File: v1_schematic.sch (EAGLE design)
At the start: 75 parts, among them IC1 PCA82C250, IC2 FT232RL, IC3 SP3223EBP, IC4 MAX481CPA, Q1 25MHz, Q2 32.768kHz, T1 ST02-3.5MM, X1 MINI-USB-32005-201

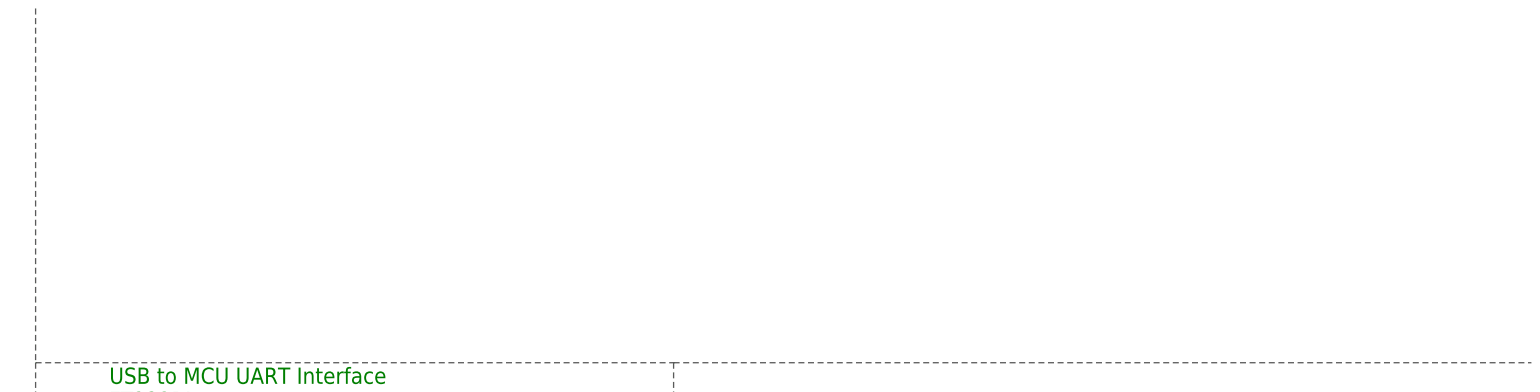
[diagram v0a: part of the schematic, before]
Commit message: Power Conversion and References
- Completed power supply conversion for 5V (VCC) and 3V3.
- Added STM32F407VETx pinout image for design reference.
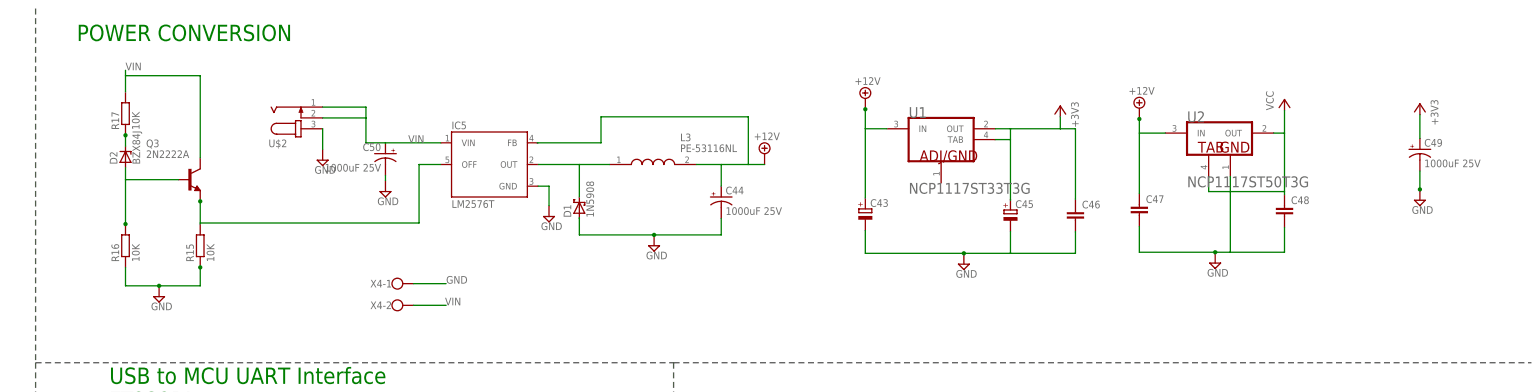
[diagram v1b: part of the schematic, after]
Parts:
- added C43, C45: (no value), rcl:CPOL-EU153CLV-1014
- added C44, C49, C50: 1000uF 25V, rcl:CPOL-USE5-6
- added C46, C47, C48: (no value), SparkFun-Capacitors:CAP0603-CAP
- added D1: 1N5908, diode:1N5908
- added D2: BZX84J, NXP_60_26022015:BZX84J
- added IC5: LM2576T, v-reg-3-new:LM2576T
- added L3: PE-53116NL, PE-53116NL:PE-53116NL
- added Q3: 2N2222A, transistor-npn:2N2222A
- added R15, R16, R17: 10K, rcl:R-EU_R0805
- added U$2: (no value), con-jack:JACK-PLUG1
- added U1: ON_SEMICONDUCTOR_NCP1117ST33T3GON_SEMICONDUCTOR_NCP1117ST33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, ON Semiconductor - NCP1117ST33T3G:ON_SEMICONDUCTOR_NCP1117ST33T3GON_SEMICONDUCTOR_NCP1117ST33T3G_0_0
- added U2: ON_SEMICONDUCTOR_NCP1117ST50T3GON_SEMICONDUCTOR_NCP1117ST50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, ON Semiconductor - NCP1117ST50T3G:ON_SEMICONDUCTOR_NCP1117ST50T3GON_SEMICONDUCTOR_NCP1117ST50T3G_0_2
- added X4: (no value), con-wago-500:W237-102
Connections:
- new net +12V: C43.+, C44.+, C47.1, L3.2, U1.IN, U2.IN
- new net N$30: D2.A, Q3.B, R16.2
- new net N$32: Q3.E, R15.2
- new net N$35: D2.C, R17.1
- new net N$36: IC5.OFF
- new net N$41: D1.C, IC5.OUT, L3.1
- new net VIN: C50.+, IC5.VIN, Q3.C, R17.2, U$2.1, U$2.2, X4-2.KL
- net +3V3: now also C46.1, C49.+, U1.OUT, U1.TAB
- net GND: now also C43.-, C44.-, C45.-, C46.2, C47.2, C48.2, C49.-, C50.-, D1.A, IC5.GND, R15.1, R16.1, U$2.3, U2.GND, X4-1.KL
- net VCC: now also C48.1, U2.OUT, U2.TAB
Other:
- note added: "POWER CONVERSION"

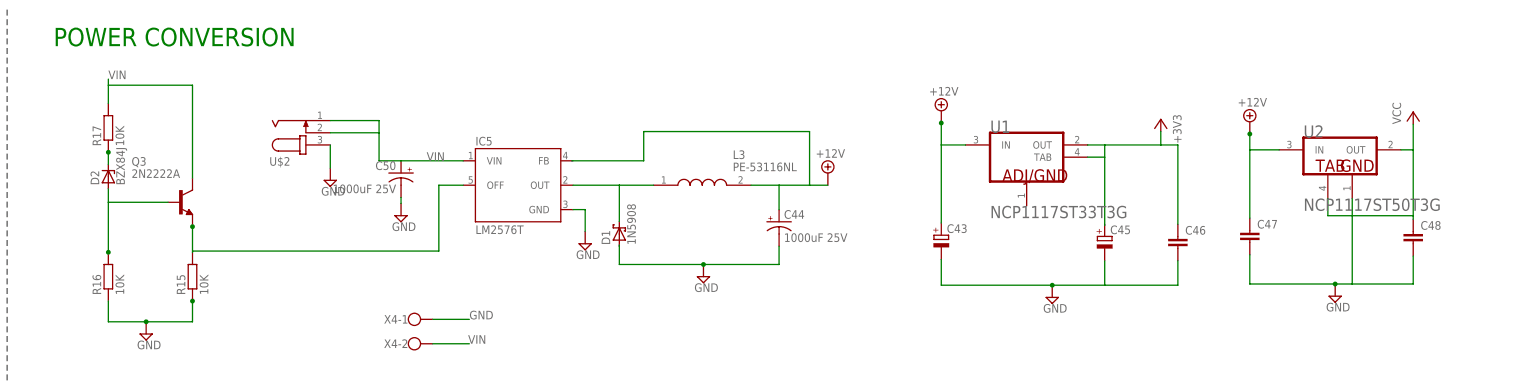
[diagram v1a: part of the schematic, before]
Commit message: Corrections
- Values for various passive parts adjusted.
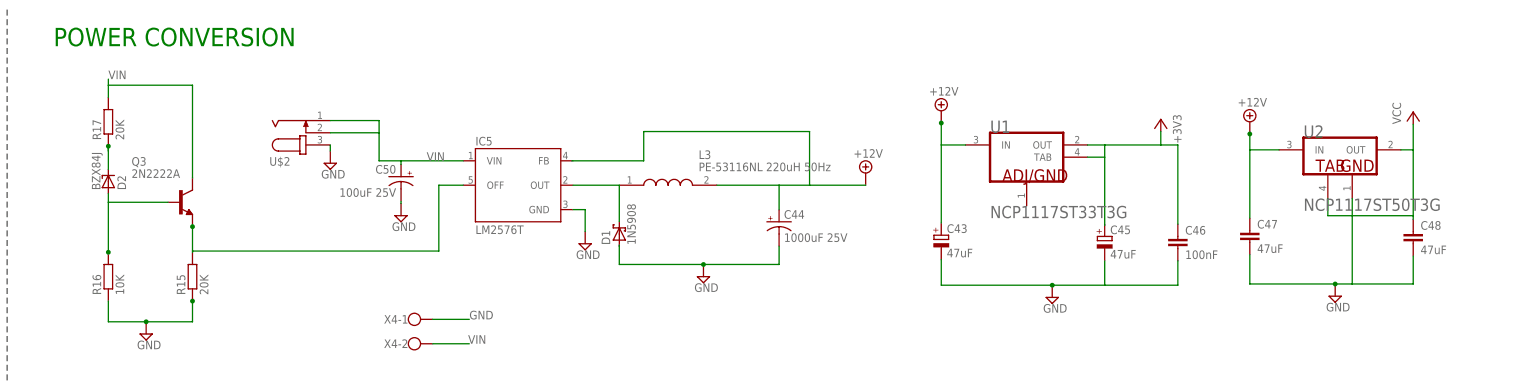
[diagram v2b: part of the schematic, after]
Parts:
- C43, C45, C47, C48: value (none) -> 47uF
- C46: value (none) -> 100nF
- C50: value 1000uF 25V -> 100uF 25V
- L3: value PE-53116NL -> PE-53116NL 220uH 50Hz
- R15, R17: value 10K -> 20K
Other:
- moved on the sheet: C50, D2, L3, R17
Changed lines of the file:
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@@
 <part name="D1" library="diode" library_urn="urn:adsk.eagle:library:210" deviceset="1N5908" device="" package3d_urn="urn:adsk.eagle:package:43355/1"/>
 <part name="Q3" library="transistor-npn" library_urn="urn:adsk.eagle:library:398" deviceset="2N2222*" device="" package3d_urn="urn:adsk.eagle:package:28973/2" technology="A"/>
-<part name="R15" library="rcl" library_urn="urn:adsk.eagle:library:334" deviceset="R-EU_" device="R0805" package3d_urn="urn:adsk.eagle:package:23553/2" value="10K"/>
+<part name="R15" library="rcl" library_urn="urn:adsk.eagle:library:334" deviceset="R-EU_" device="R0805" package3d_urn="urn:adsk.eagle:package:23553/2" value="20K"/>
 <part name="R16" library="rcl" library_urn="urn:adsk.eagle:library:334" deviceset="R-EU_" device="R0805" package3d_urn="urn:adsk.eagle:package:23553/2" value="10K"/>
-<part name="R17" library="rcl" library_urn="urn:adsk.eagle:library:334" deviceset="R-EU_" device="R0805" package3d_urn="urn:adsk.eagle:package:23553/2" value="10K"/>
+<part name="R17" library="rcl" library_urn="urn:adsk.eagle:library:334" deviceset="R-EU_" device="R0805" package3d_urn="urn:adsk.eagle:package:23553/2" value="20K"/>
 <part name="D2" library="NXP_60_26022015" deviceset="BZX84J" device=""/>
-<part name="C43" library="rcl" library_urn="urn:adsk.eagle:library:334" deviceset="CPOL-EU" device="153CLV-1014" package3d_urn="urn:adsk.eagle:package:23406/1"/>
+<part name="C43" library="rcl" library_urn="urn:adsk.eagle:library:334" deviceset="CPOL-EU" device="153CLV-1014" package3d_urn="urn:adsk.eagle:package:23406/1" value="47uF"/>
 <part name="C44" library="rcl" library_urn="urn:adsk.eagle:library:334" deviceset="CPOL-US" device="E5-6" package3d_urn="urn:adsk.eagle:package:23368/1" value="1000uF 25V"/>
-<part name="L3" library="PE-53116NL" deviceset="PE-53116NL" device=""/>
-<part name="C45" library="rcl" library_urn="urn:adsk.eagle:library:334" deviceset="CPOL-EU" device="153CLV-1014" package3d_urn="urn:adsk.eagle:package:23406/1"/>
-<part name="C46" library="SparkFun-Capacitors" deviceset="CAP" device="0603-CAP"/>
-<part name="C47" library="SparkFun-Capacitors" deviceset="CAP" device="0603-CAP"/>
-<part name="C48" library="SparkFun-Capacitors" deviceset="CAP" device="0603-CAP"/>
+<part name="L3" library="PE-53116NL" deviceset="PE-53116NL" device="" value="PE-53116NL 220uH 50Hz"/>
+<part name="C45" library="rcl" library_urn="urn:adsk.eagle:library:334" deviceset="CPOL-EU" device="153CLV-1014" package3d_urn="urn:adsk.eagle:package:23406/1" value="47uF"/>
+<part name="C46" library="SparkFun-Capacitors" deviceset="CAP" device="0603-CAP" value="100nF"/>
+<part name="C47" library="SparkFun-Capacitors" deviceset="CAP" device="0603-CAP" value="47uF"/>
+<part name="C48" library="SparkFun-Capacitors" deviceset="CAP" device="0603-CAP" value="47uF"/>
 <part name="C49" library="rcl" library_urn="urn:adsk.eagle:library:334" deviceset="CPOL-US" device="E5-6" package3d_urn="urn:adsk.eagle:package:23368/1" value="1000uF 25V"/>
 <part name="U$2" library="con-jack" library_urn="urn:adsk.eagle:library:154" deviceset="JACK-PLUG" device="1" package3d_urn="urn:adsk.eagle:package:7494/1"/>
-<part name="C50" library="rcl" library_urn="urn:adsk.eagle:library:334" deviceset="CPOL-US" device="E5-6" package3d_urn="urn:adsk.eagle:package:23368/1" value="1000uF 25V"/>
+<part name="C50" library="rcl" library_urn="urn:adsk.eagle:library:334" deviceset="CPOL-US" device="E5-6" package3d_urn="urn:adsk.eagle:package:23368/1" value="100uF 25V"/>
 <part name="X4" library="con-wago-500" library_urn="urn:adsk.eagle:library:195" deviceset="W237-102" device="" package3d_urn="urn:adsk.eagle:package:10688/1"/>
 <part name="SUPPLY23" library="supply2" library_urn="urn:adsk.eagle:library:372" deviceset="GND" device=""/>
@@
 <instance part="R15" gate="G$1" x="-51.308" y="147.32" rot="R90"/>
 <instance part="R16" gate="G$1" x="-68.834" y="147.32" rot="R90"/>
-<instance part="R17" gate="G$1" x="-68.834" y="178.308" rot="R90"/>
-<instance part="D2" gate="G$1" x="-68.834" y="168.148" rot="R90"/>
+<instance part="R17" gate="G$1" x="-68.834" y="179.578" rot="R90"/>
+<instance part="D2" gate="G$1" x="-68.834" y="167.132" rot="MR90"/>
 <instance part="C43" gate="G$1" x="104.648" y="155.956"/>
 <instance part="C44" gate="G$1" x="70.866" y="158.75"/>
-<instance part="L3" gate="G$1" x="44.704" y="166.37"/>
+<instance part="L3" gate="G$1" x="37.592" y="166.37"/>
 <instance part="C45" gate="G$1" x="138.684" y="155.702"/>
 <instance part="C46" gate="G$1" x="153.924" y="153.162"/>
@@
 <instance part="C49" gate="G$1" x="234.696" y="169.926"/>
 <instance part="U$2" gate="G$1" x="-27.686" y="177.292" rot="MR180"/>
-<instance part="C50" gate="G$1" x="-7.874" y="168.91" rot="MR0"/>
+<instance part="C50" gate="G$1" x="-7.874" y="168.148" rot="MR0"/>
 <instance part="X4" gate="-1" x="-6.35" y="138.43"/>
 <instance part="X4" gate="-2" x="-6.35" y="133.35"/>
@@
 <instance part="+3V9" gate="G$1" x="150.368" y="180.086" rot="MR0"/>
 <instance part="+3V10" gate="G$1" x="234.696" y="180.594" rot="MR0"/>
-<instance part="SUPPLY30" gate="+12V" x="81.026" y="168.91"/>
+<instance part="SUPPLY30" gate="+12V" x="88.9" y="168.91"/>
 <instance part="SUPPLY31" gate="+12V" x="104.648" y="181.864"/>
 <instance part="SUPPLY32" gate="+12V" x="168.91" y="179.578"/>
-<instance part="SUPPLY33" gate="GND" x="-22.606" y="167.386"/>
+<instance part="SUPPLY33" gate="GND" x="-22.606" y="170.942"/>
 </instances>
 <busses>
@@
 <pinref part="SUPPLY28" gate="GND" pin="GND"/>
 <pinref part="C50" gate="G$1" pin="-"/>
-<wire x1="-7.874" y1="162.56" x2="-7.874" y2="163.83" width="0.1524" layer="91"/>
+<wire x1="-7.874" y1="162.56" x2="-7.874" y2="163.068" width="0.1524" layer="91"/>
 </segment>
 <segment>
@@
 <segment>
 <pinref part="U$2" gate="G$1" pin="3"/>
-<wire x1="-22.606" y1="174.752" x2="-22.606" y2="169.926" width="0.1524" layer="91"/>
+<wire x1="-22.606" y1="174.752" x2="-22.606" y2="173.482" width="0.1524" layer="91"/>
 <pinref part="SUPPLY33" gate="GND" pin="GND"/>
 </segment>
@@
 <pinref part="Q3" gate="G$1" pin="B"/>
 <wire x1="-68.834" y1="152.4" x2="-68.834" y2="162.814" width="0.1524" layer="91"/>
-<wire x1="-68.834" y1="162.814" x2="-68.834" y2="165.608" width="0.1524" layer="91"/>
+<wire x1="-68.834" y1="162.814" x2="-68.834" y2="164.592" width="0.1524" layer="91"/>
 <wire x1="-56.388" y1="162.814" x2="-68.834" y2="162.814" width="0.1524" layer="91"/>
 <pinref part="R16" gate="G$1" pin="2"/>
@@
 <segment>
 <pinref part="D2" gate="G$1" pin="C"/>
-<wire x1="-68.834" y1="173.482" x2="-68.834" y2="173.228" width="0.1524" layer="91"/>
+<wire x1="-68.834" y1="173.482" x2="-68.834" y2="174.498" width="0.1524" layer="91"/>
 <pinref part="R17" gate="G$1" pin="1"/>
-<wire x1="-68.834" y1="173.228" x2="-68.834" y2="170.688" width="0.1524" layer="91"/>
-<junction x="-68.834" y="173.228"/>
+<wire x1="-68.834" y1="174.498" x2="-68.834" y2="169.672" width="0.1524" layer="91"/>
+<junction x="-68.834" y="174.498"/>
 </segment>
 </net>
@@
 <wire x1="-22.606" y1="179.832" x2="-12.446" y2="179.832" width="0.1524" layer="91"/>
 <wire x1="-12.446" y1="179.832" x2="-12.446" y2="177.292" width="0.1524" layer="91"/>
-<pinref part="C50" gate="G$1" pin="+"/>
 <wire x1="-12.446" y1="177.292" x2="-12.446" y2="171.45" width="0.1524" layer="91"/>
-<wire x1="-12.446" y1="171.45" x2="-7.874" y2="171.45" width="0.1524" layer="91"/>
-<pinref part="IC5" gate="A" pin="VIN"/>
-<wire x1="-7.874" y1="171.45" x2="5.08" y2="171.45" width="0.1524" layer="91"/>
 <pinref part="U$2" gate="G$1" pin="2"/>
 <wire x1="-22.606" y1="177.292" x2="-12.446" y2="177.292" width="0.1524" layer="91"/>
 <label x="-2.54" y="171.45" size="1.778" layer="95"/>
+<wire x1="-12.446" y1="171.45" x2="-7.874" y2="171.45" width="0.1524" layer="91"/>
+<pinref part="C50" gate="G$1" pin="+"/>
+<wire x1="-7.874" y1="170.688" x2="-7.874" y2="171.45" width="0.1524" layer="91"/>
+<pinref part="IC5" gate="A" pin="VIN"/>
+<wire x1="-7.874" y1="171.45" x2="5.08" y2="171.45" width="0.1524" layer="91"/>
 </segment>
 <segment>
@@
 <wire x1="-51.308" y1="187.198" x2="-68.834" y2="187.198" width="0.1524" layer="91"/>
 <pinref part="R17" gate="G$1" pin="2"/>
-<wire x1="-68.834" y1="187.198" x2="-68.834" y2="183.388" width="0.1524" layer="91"/>
+<wire x1="-68.834" y1="187.198" x2="-68.834" y2="184.658" width="0.1524" layer="91"/>
 <wire x1="-68.834" y1="187.198" x2="-68.834" y2="188.468" width="0.1524" layer="91"/>
 <label x="-68.834" y="188.468" size="1.778" layer="95"/>
@@
 <wire x1="37.592" y1="158.75" x2="37.592" y2="166.37" width="0.1524" layer="91"/>
 <pinref part="IC5" gate="A" pin="OUT"/>
-<wire x1="37.592" y1="166.37" x2="44.704" y2="166.37" width="0.1524" layer="91"/>
 <wire x1="27.94" y1="166.37" x2="37.592" y2="166.37" width="0.1524" layer="91"/>
 </segment>
@@
 <pinref part="L3" gate="G$1" pin="2"/>
 <pinref part="C44" gate="G$1" pin="+"/>
-<wire x1="65.024" y1="166.37" x2="70.866" y2="166.37" width="0.1524" layer="91"/>
+<wire x1="57.912" y1="166.37" x2="70.866" y2="166.37" width="0.1524" layer="91"/>
 <wire x1="70.866" y1="166.37" x2="70.866" y2="161.29" width="0.1524" layer="91"/>
-<wire x1="81.026" y1="166.37" x2="77.216" y2="166.37" width="0.1524" layer="91"/>
+<wire x1="88.9" y1="166.37" x2="77.216" y2="166.37" width="0.1524" layer="91"/>
 <wire x1="77.216" y1="166.37" x2="70.866" y2="166.37" width="0.1524" layer="91"/>
 <wire x1="77.216" y1="166.37" x2="77.216" y2="177.546" width="0.1524" layer="91"/>

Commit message: Ethernet Interface
- added SPI ethernet module interface on SPI1, where MCU is SPI_master while W5100/W5500 module is SPI_slave
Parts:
- added JP1: (no value), pinhead:PINHD-1X10
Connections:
- net N4 renamed SPI1_SS
- removed net P3: U$1.PA6
- removed net P4: U$1.PA5
- removed net R3: U$1.PA7
- new net SPI1_MISO: JP1.6, U$1.PA6
- new net SPI1_MOSI: JP1.8, U$1.PA7
- new net SPI1_SCK: JP1.4, U$1.PA5
- net GND: now also C6.2, JP1.10, JP1.3, JP1.5, JP1.7, JP1.9
- net VCC: now also R5.1
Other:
- note added: "Ethernet Module Interface (W5100 Chip)"
- moved on the sheet: C5, C6, C7, C8, C9, IC2, L1, LED2, LED3, R5, R6, X1

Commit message: RS232 Interface
- Added protection circuitry
- Corrected a few connections
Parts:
- added JP2: (no value), pinhead:PINHD-1X10
- added R18, R19, R28: 10K, rcl:R-EU_R0805
- added R20, R21, R22: 4k7, rcl:R-EU_R0805
- added R23, R24, R25, R26, R27: 1k, resistor:R-EU_R0805
- added T3, T4, T5, T6, T7: 2N2222, transistor-neu-to92:2N2222
- added X5: (no value), con-wago-500:W237-6
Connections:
- new net GND2: T7.C, X2.5, X5-6.KL
- new net N$31: R22.1, R28.2
- new net N$49: R23.1
- new net N$51: R24.1
- new net N$52: R25.1
- new net N$54: R26.1
- new net R1IN_: T6.C, X5-5.KL
- new net R2IN_: T4.C, X5-4.KL
- new net T1OUT_: T5.C, X5-3.KL
- new net T20UT_: X5-2.KL
- new net T2OUT_: T3.C
- net +3V3: now also JP1.1, R24.2, R25.2
- net GND: now also R18.1, R19.1, R20.1, R21.1, T7.E; no longer X2.5
- net N$4: now also R22.2
- net N$9: no longer IC2.3V3OUT
- net R1IN: now also T6.E
- net R2IN: now also T4.E
- net SPI1_SS: now also JP1.2
- net T1OUT: now also T5.E
- net T2OUT: now also T3.E
- net UART4_RX: now also R18.2
- net UART4_TX: now also R19.2
- net VCC: now also X5-1.KL
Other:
- note added: "Ethernet Module Interface (W5100/W5500 Chip)"
- note added: "nRF5 Module Interface (nRF51822 Chip)"
- note removed: "Ethernet Module Interface (W5100 Chip)"
- moved on the sheet: C10, C11, C12, C13, C42, C5, C6, C7, C8, C9, IC1, IC2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
